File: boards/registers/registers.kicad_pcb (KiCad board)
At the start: 2 copper layers, 100 x 100 mm, 216 parts, among them J1 SSW-120-02-G-D-RA, J2 SSW-120-02-G-D-RA, J5 SSW-120-02-G-D-RA, SW1 RESET, SW2 STEP, SW3 OS102011MS2QN1, U1 SN74LV08APW, U10 74HC161PW, U11 MC74HC244ADT, U12 MC74HC244ADT, U13 74HC161PW, U14 74HC161PW, U15 MC74HC244ADT, U16 MC74HC244ADT, U17 74HC161PW, U18 74HC161PW, U19 MC74HC244ADT, U2 MC74HC244ADT, U20 MC74HC244ADT, U21 74HC161PW, U22 74HC161PW, U23 MC74HC244ADT, U24 MC74HC244ADT, U25 MC74HC273ADT, U26 MC74HC244ADT, U27 MC74HC244ADT, U28 MC74HC273ADT, U29 MC74HC244ADT, U3 MC74HC273ADT, U30 74HC74PW, U31 SN74AHC1G86DBVR, U34 SN74LV14APW, U4 74HC161PW, U5 SN74LV86APWR, U6 SN74LV08APW, U7 SN74LV32APWR, U8 SN74LV32APWR, U9 74HC161PW

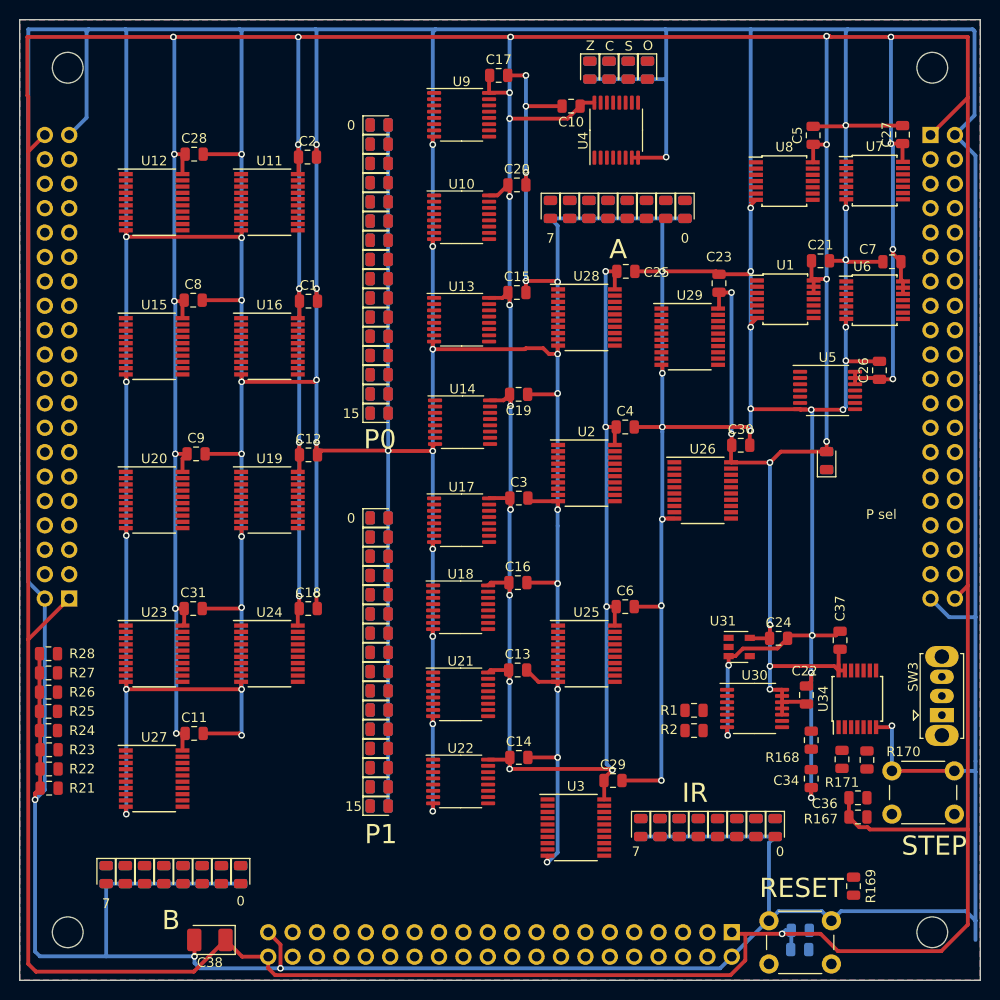
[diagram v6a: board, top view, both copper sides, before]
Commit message: Registers board rev. 2
Implement RDY mechanism by suspending clock signal
Take caution against crosstalk on sensitive line
Add proper decoupling capacitors
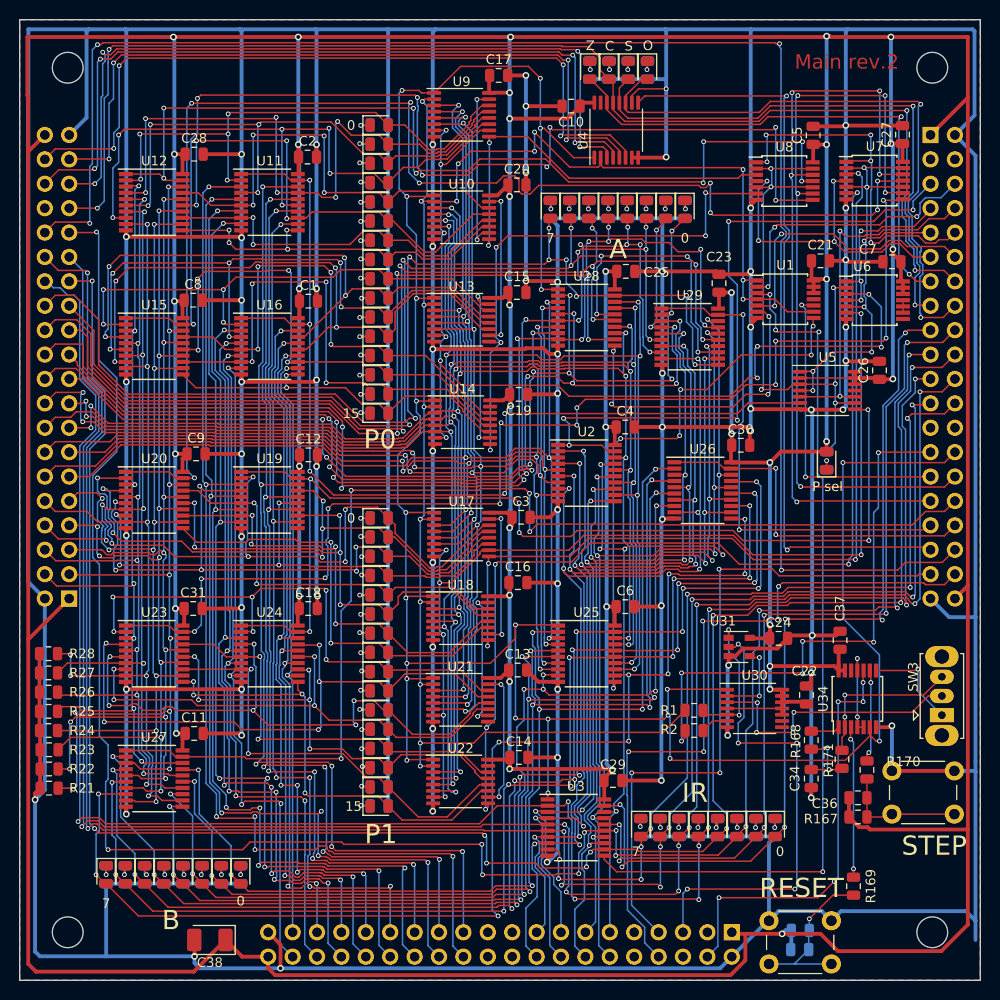
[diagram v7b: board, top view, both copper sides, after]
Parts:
- moved C3 2.01 mm to (152.2, 101.8)
- moved U17 1.50 mm to (146.0, 103.6)
- moved U18 1.13 mm to (145.9, 112.3)
- moved R170 1.04 mm to (188.2, 128.1)
- moved U21 0.57 mm to (145.9, 120.8)
- turned R171 to 270 degrees
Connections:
- net Net-(U1-Pad3) renamed /ir_w_clk
- J5 pad 3: /clk -> (no net)
- U2 pad 11: /d7 -> /d3
- U2 pad 12: /di3 -> /di7
- U2 pad 13: /d6 -> /d2
- U2 pad 14: /di2 -> /di6
- U2 pad 15: /d5 -> /d1
- U2 pad 16: /di1 -> /di5
- U2 pad 17: /d4 -> /d0
- U2 pad 18: /di0 -> /di4
- U2 pad 2: /d0 -> /d4
- U2 pad 3: /di4 -> /di0
- U2 pad 4: /d1 -> /d5
- U2 pad 5: /di5 -> /di1
- U2 pad 6: /d2 -> /d6
- U2 pad 7: /di6 -> /di2
- U2 pad 8: /d3 -> /d7
- U2 pad 9: /di7 -> /di3
- U27 pad 11: /gp_reg_b/d7 -> /gp_reg_b/d3
- U27 pad 12: /alu_b3 -> /alu_b7
- U27 pad 13: /gp_reg_b/d6 -> /gp_reg_b/d2
- U27 pad 14: /alu_b2 -> /alu_b6
- U27 pad 15: /gp_reg_b/d5 -> /gp_reg_b/d1
- U27 pad 16: /alu_b1 -> /alu_b5
- U27 pad 17: /gp_reg_b/d4 -> /gp_reg_b/d0
- U27 pad 18: /alu_b0 -> /alu_b4
- U27 pad 2: /gp_reg_b/d0 -> /gp_reg_b/d4
- U27 pad 3: /alu_b4 -> /alu_b0
- U27 pad 4: /gp_reg_b/d1 -> /gp_reg_b/d5
- U27 pad 5: /alu_b5 -> /alu_b1
- U27 pad 6: /gp_reg_b/d2 -> /gp_reg_b/d6
- U27 pad 7: /alu_b6 -> /alu_b2
- U27 pad 8: /gp_reg_b/d3 -> /gp_reg_b/d7
- U27 pad 9: /alu_b7 -> /alu_b3
- U3 pad 12: /alu_op1 -> /alu_op0
- U3 pad 13: /d4 -> /d3
- U3 pad 14: /d5 -> /d2
- U3 pad 15: /alu_op2 -> /alu_invert
- U3 pad 16: /alu_op3 -> /ir_out1
- U3 pad 17: /d6 -> /d1
- U3 pad 18: /d7 -> /d0
- U3 pad 19: /ir_out7 -> /ir_out0
- U3 pad 2: /alu_op0 -> /alu_op1
- U3 pad 3: /d3 -> /d4
- U3 pad 4: /d2 -> /d5
- U3 pad 5: /alu_invert -> /alu_op2
- U3 pad 6: /ir_out1 -> /alu_op3
- U3 pad 7: /d1 -> /d6
- U3 pad 8: /d0 -> /d7
- U3 pad 9: /ir_out0 -> /ir_out7
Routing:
- net /~rst: track 0.00 -> 270.9 mm, vias 0 -> 21
- net /alu_invert: track 0.00 -> 214.9 mm, vias 0 -> 12
- net /alu_op1: track 0.00 -> 214.1 mm, vias 0 -> 9
- net /alu_op2: track 0.00 -> 212.2 mm, vias 0 -> 9
- net /alu_op3: track 0.00 -> 207.7 mm, vias 0 -> 10
- net /alu_op0: track 0.00 -> 205.5 mm, vias 0 -> 10
- net /di7: track 0.00 -> 180.0 mm, vias 0 -> 11
- net /di3: track 0.00 -> 176.3 mm, vias 0 -> 11
- net /di1: track 0.00 -> 174.6 mm, vias 0 -> 10
- net /di2: track 0.00 -> 173.6 mm, vias 0 -> 10
- net /~clk: track 0.00 -> 173.3 mm, vias 0 -> 16
- net /di6: track 0.00 -> 173.3 mm, vias 0 -> 11
- net /di5: track 0.00 -> 171.0 mm, vias 0 -> 9
- net /~oe_alu: track 0.00 -> 169.5 mm, vias 0 -> 4
- net /di4: track 0.00 -> 167.7 mm, vias 0 -> 11
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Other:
- board text added: "Main rev.2"
